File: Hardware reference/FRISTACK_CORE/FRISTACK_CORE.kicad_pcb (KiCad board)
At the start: 2 copper layers, 51 x 51 mm, 93 parts, among them J1 Conn_01x13_Socket, J2 USB_C_Receptacle_USB2.0_16P, J3 Conn_01x13_Socket, J6 JTAG_PIN_HEADER, SW1 SW_DIP_x01, SW2 SW_DIP_x01, U1 USBLC6-2SC6, U2 MCP73871-2CC, U3 TPS62840DLCR, U4 ESP32-S3-MINI-1U, U5 FSUSB42MUX, U6 SN65HVD232, Y1 32.768 kHz

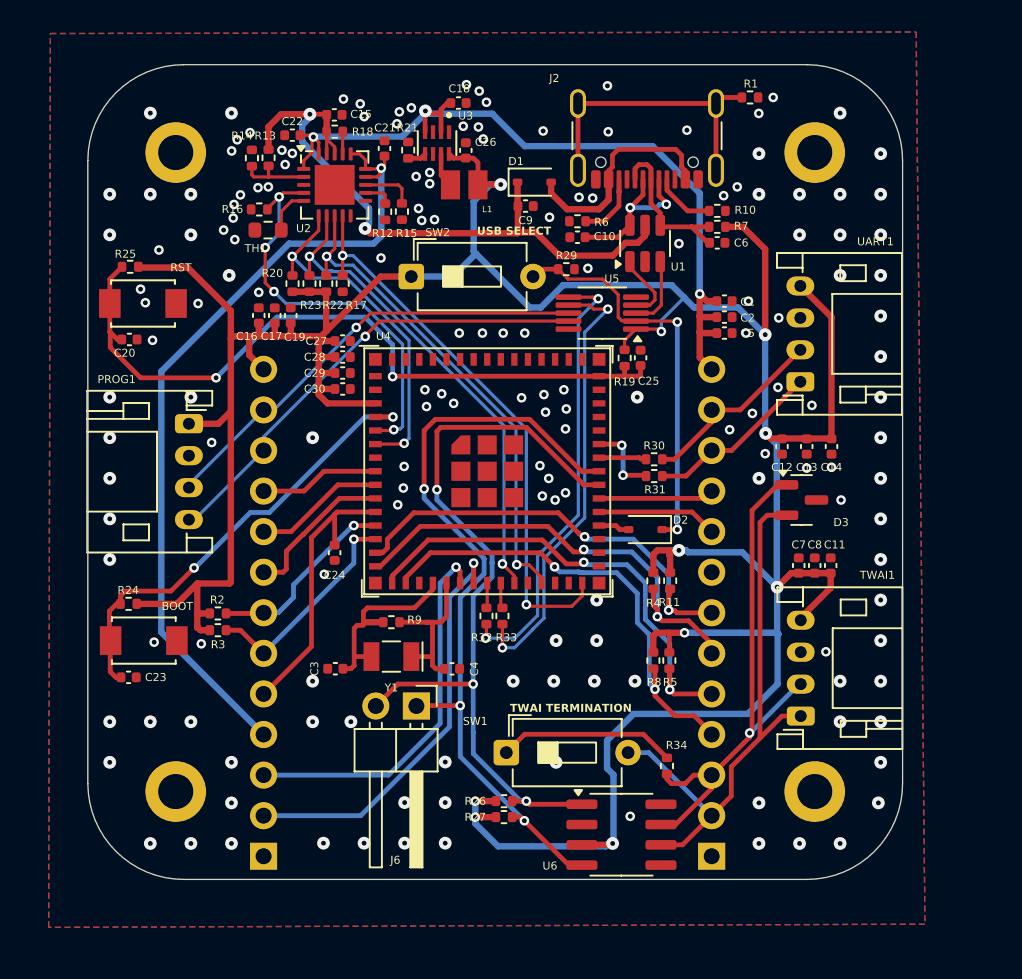
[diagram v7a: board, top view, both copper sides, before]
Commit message: Changes to Core and Sensor Node
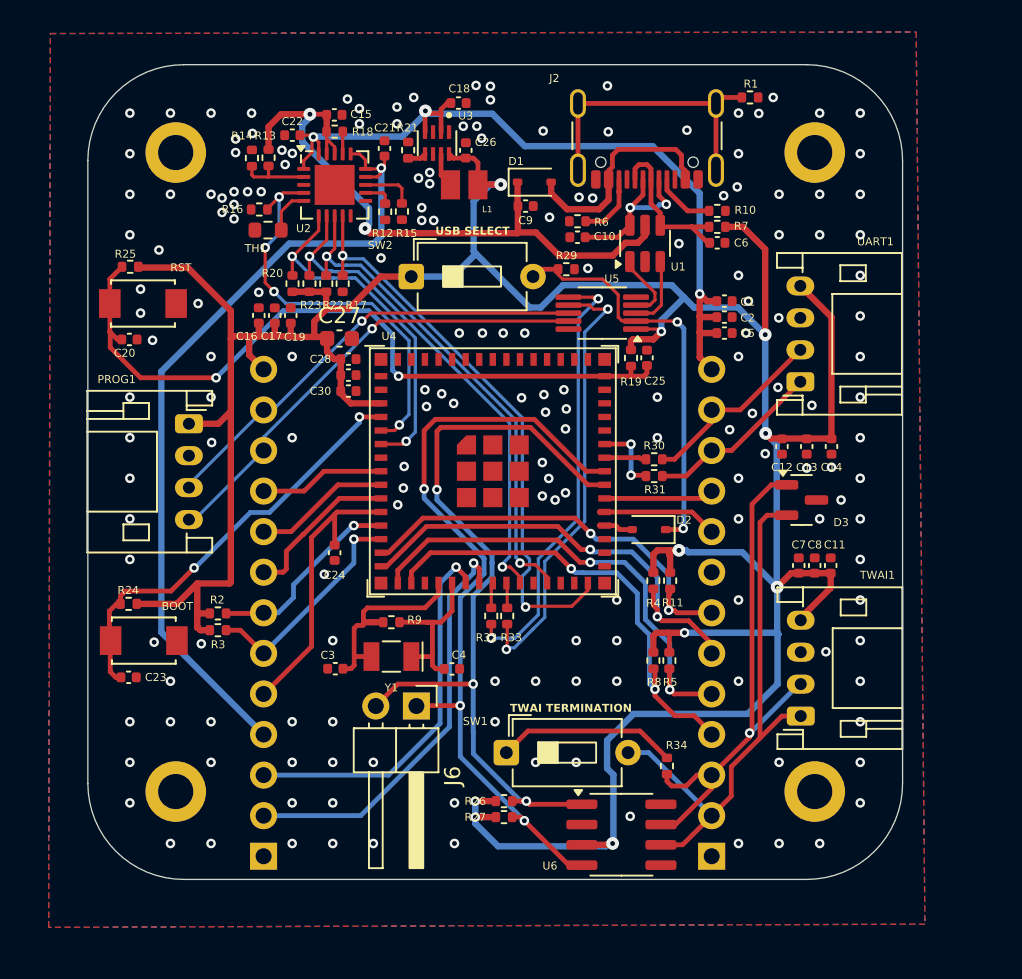
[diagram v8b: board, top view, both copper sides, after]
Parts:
- C27: footprint Capacitor_SMD:C_0402_1005Metric -> Capacitor_SMD:C_0603_1608Metric
- moved C25 0.40 mm to (162.0, 90.3)
- moved R19 0.40 mm to (161.0, 90.4)
- moved C28 0.38 mm to (143.3, 90.4)
- moved C29 0.38 mm to (143.3, 91.4)
- moved C30 0.38 mm to (143.3, 92.4)
- moved U4 0.35 mm to (152.3, 97.5)
- moved R32 0.30 mm to (152.2, 106.5)
- moved R33 0.30 mm to (153.2, 106.5)
- moved C27 0.26 mm to (142.8, 89.1)
- moved D2 0.22 mm to (162.1, 101.1)
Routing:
- net ESP_PWR: track 221.1 -> 218.2 mm
- net GPIO0: track 28.8 -> 27.2 mm
- net GPIO48: track 35.3 -> 36.5 mm
- net STAT2: track 31.0 -> 32.0 mm
- net CS: track 27.4 -> 26.5 mm
- net EN: track 45.8 -> 46.6 mm
- net MISO: track 29.4 -> 28.9 mm
- net X_TAL_P: track 11.6 -> 12.1 mm
- net GND: vias 165 -> 180
